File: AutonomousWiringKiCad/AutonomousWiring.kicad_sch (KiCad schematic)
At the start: 19 parts

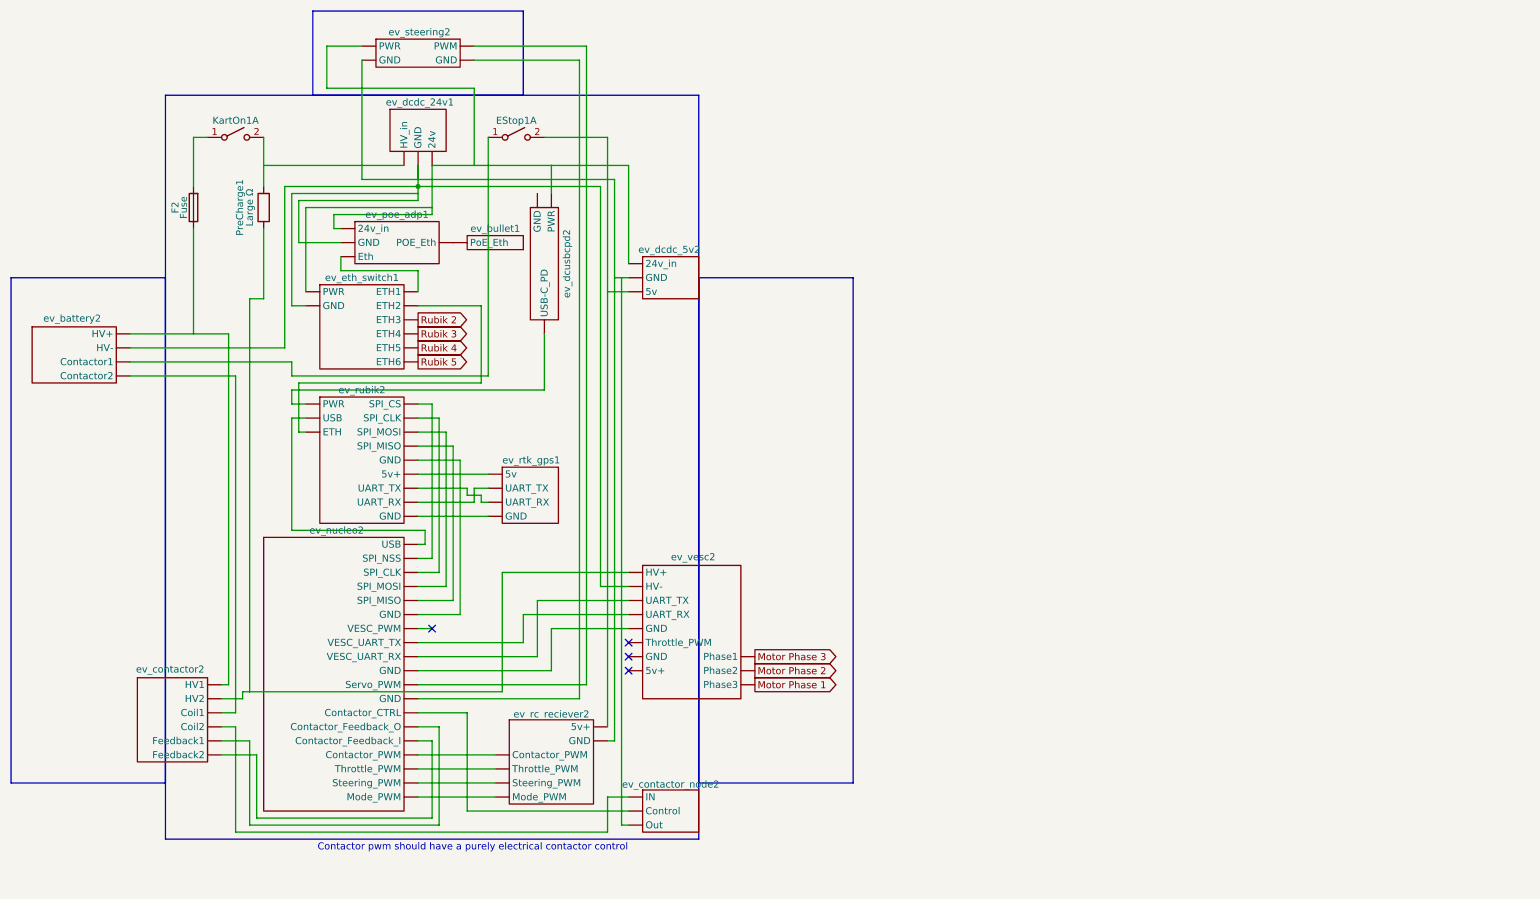
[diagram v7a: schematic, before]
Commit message: changing the contactor node to be nmos? PWM direct estop
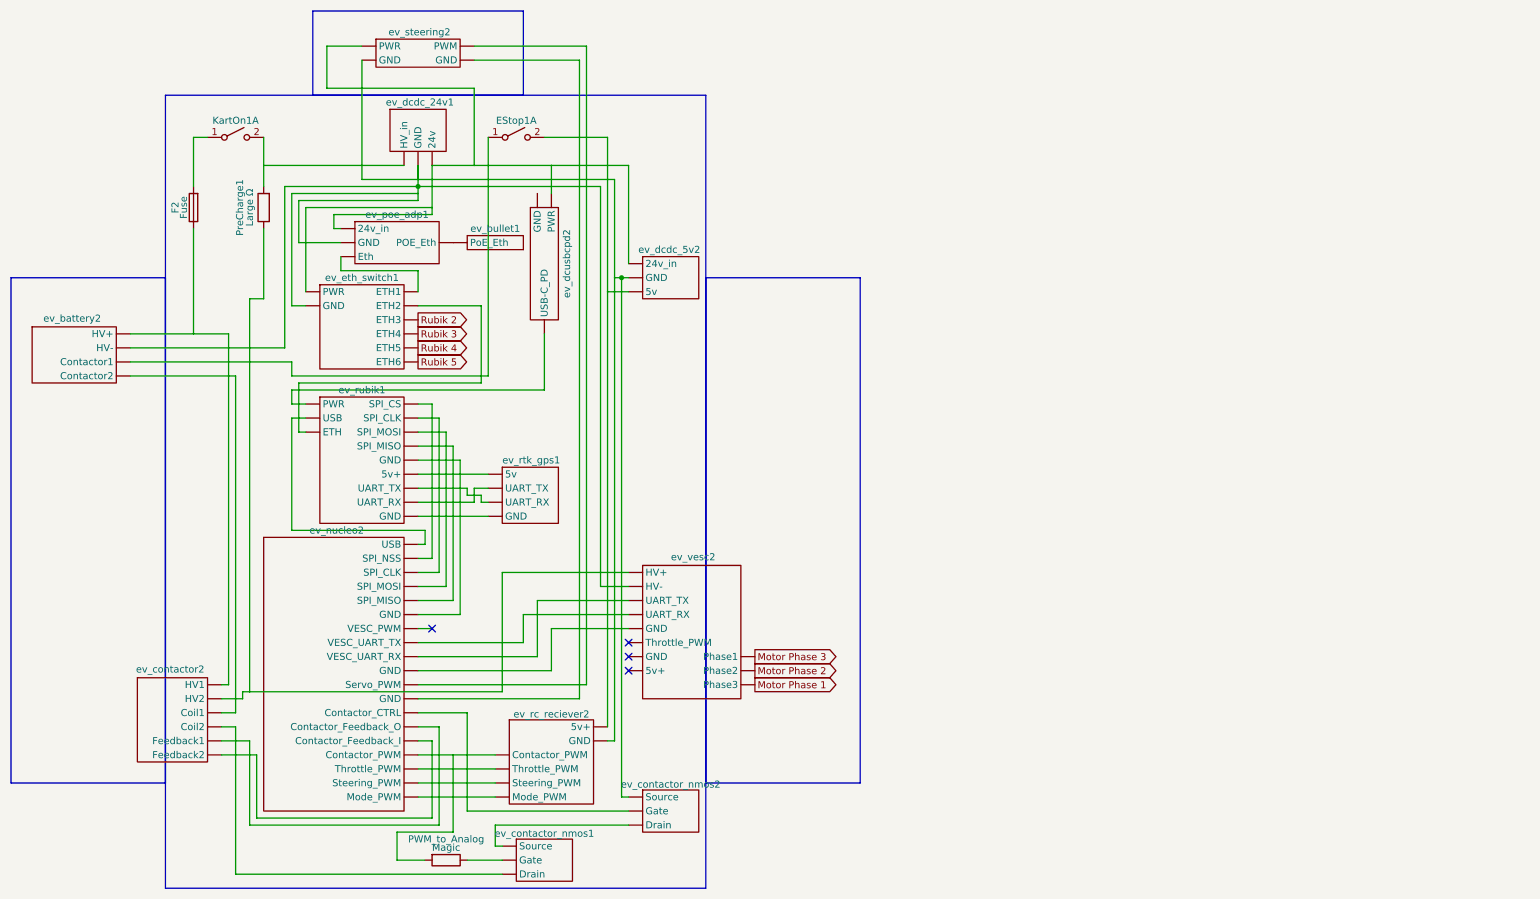
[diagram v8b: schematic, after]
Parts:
- added PWM_to_Analog: Magic, symbol Device:R
- added ev_contactor_nmos1: ~, symbol ev_kart:ev_contactor_node
- renumbered ev_contactor_node2 to ev_contactor_nmos2, ev_rubik2 to ev_rubik1
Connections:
- net at ev_nucleo2. (Mode_PWM): now also ev_vesc2. (Phase3)
- net at ev_contactor_nmos2. (Drain): now also ev_contactor_nmos1. (Drain); no longer ev_nucleo2. (Mode_PWM)
- net at ev_contactor2. (Feedback2): now also ev_contactor_nmos1. (Drain); no longer ev_nucleo2. (Mode_PWM)
- net at ev_rc_reciever2. (GND): now also EStop1.2 (B), ev_dcdc_5v2. (5v); no longer ev_nucleo2. (Mode_PWM)
- net at ev_rubik1. (GND): now also ev_dcusbcpd2. (USB-C_PD); no longer ev_nucleo2. (Mode_PWM)
- net at ev_poe_adp1. (POE_Eth): now also ev_bullet1. (PoE_Eth); no longer ev_eth_switch1. (ETH6)
- net at ev_battery2. (Contactor2): now also EStop1.1 (A); no longer ev_contactor2. (Feedback2)
- new net: ev_battery2. (Contactor2), ev_contactor_nmos2. (Drain), ev_dcdc_24v1. (24v), ev_dcdc_5v2. (5v), ev_eth_switch1. (ETH6), ev_poe_adp1. (POE_Eth), ev_rc_reciever2. (GND), ev_steering2. (GND), ev_vesc2. (Phase3)
- new net: ev_dcdc_24v1. (24v), ev_dcdc_5v2. (5v), ev_dcusbcpd2. (USB-C_PD), ev_eth_switch1. (ETH6), ev_poe_adp1. (POE_Eth), ev_steering2. (GND)
- new net: ev_contactor_nmos2. (Drain), ev_nucleo2. (Mode_PWM)
- new net: ev_nucleo2. (Mode_PWM), ev_steering2. (GND)
- new net: ev_contactor2. (Feedback2), ev_nucleo2. (Mode_PWM) (x2)
- new net: PWM_to_Analog.2, ev_nucleo2. (Mode_PWM), ev_rc_reciever2. (GND)
- new net: ev_nucleo2. (Mode_PWM), ev_rc_reciever2. (GND) (x3)
- new net: ev_nucleo2. (Mode_PWM), ev_rubik1. (GND) (x6)
- new net: ev_nucleo2. (Mode_PWM), ev_vesc2. (Phase3) (x2)
- new net: F2.1, ev_battery2. (Contactor2), ev_contactor2. (Feedback2)
- new net: ev_eth_switch1. (ETH6), ev_poe_adp1. (POE_Eth)
- new net: ev_battery2. (Contactor2), ev_contactor2. (Feedback2)
- new net: PreCharge1.1, ev_contactor2. (Feedback2), ev_vesc2. (Phase3)
- new net: ev_eth_switch1. (ETH6), ev_rubik1. (GND)
- new net: ev_rtk_gps1. (GND), ev_rubik1. (GND) (x3)
- new net: PWM_to_Analog.1, ev_contactor_nmos1. (Drain)
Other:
- note removed: "Contactor pwm should have a purely electrical contactor control"
